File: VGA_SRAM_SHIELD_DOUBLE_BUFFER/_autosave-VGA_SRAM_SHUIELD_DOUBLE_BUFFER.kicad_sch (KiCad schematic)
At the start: 45 parts, among them J1 USB_A_Stacked, J2 ANALOG, J3 Mini-DIN-6, J4 PWR AUX, J5 ISP, J6 Micro_SD_Card, J7 VGA D-SUB15, J8 AUDIO, U1 74HC245, U10 74HC245, U11 74HC245, U12 74LS08, U13 74LS32, U14 DATA_BANK1, U15 DATA_BANK2, U16 74HC245, U17 74HC245, U18 74HC245, U19 K6X8008T2B-TF55, U2 74HC245, U20 K6X8008T2B-TF55, U21 74HC245, U22 74HC245, U3 74HC245, U4 ATF1504AS, U5 74HC245, U6 74HC245, U7 74HC245, U8 74HC14, U9 74HC245, X1 TCXO-14

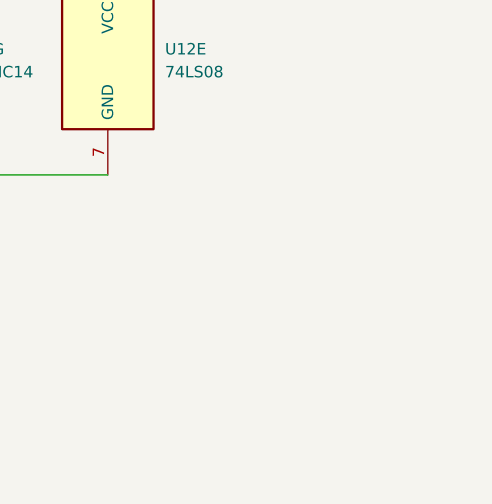
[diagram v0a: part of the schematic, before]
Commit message: remove second vga resistor network
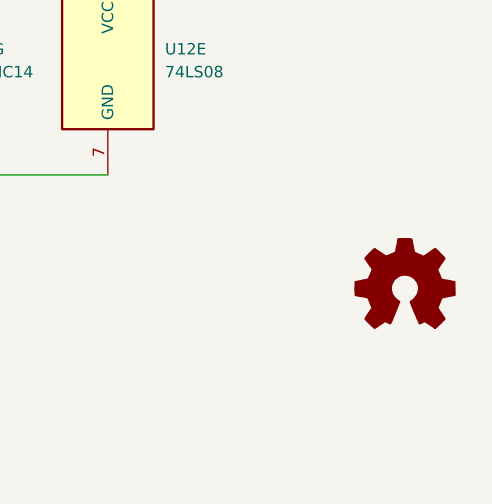
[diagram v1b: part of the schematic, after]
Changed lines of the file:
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@@
+	)
+	(symbol
+		(lib_id "Graphic:Logo_Open_Hardware_Small")
+		(at 571.5 383.54 0)
+		(unit 1)
+		(exclude_from_sim no)
+		(in_bom no)
+		(on_board no)
+		(dnp no)
+		(fields_autoplaced yes)
+		(property "Reference" "#SYM1"
+			(at 571.5 376.555 0)
+			(effects
+				(font
+					(size 1.27 1.27)
+				)
+				(hide yes)
+			)
+		)
+		(property "Value" "Logo_Open_Hardware_Small"
+			(at 571.5 389.255 0)
+			(effects
+				(font
+					(size 1.27 1.27)
+				)
+				(hide yes)
+			)
+		)
+		(property "Footprint" ""
+			(at 571.5 383.54 0)
+			(effects
+				(font
+					(size 1.27 1.27)
+				)
+				(hide yes)
+			)
+		)
+		(property "Datasheet" "~"
+			(at 571.5 383.54 0)
+			(effects
+				(font
+					(size 1.27 1.27)
+				)
+				(hide yes)
+			)
+		)
+		(property "Description" "Open Hardware logo, small"
+			(at 571.5 383.54 0)
+			(effects
+				(font
+					(size 1.27 1.27)
+				)
+				(hide yes)
+			)
+		)
+		(property "Sim.Enable" "0"
+			(at 571.5 383.54 0)
+			(effects
+				(font
+					(size 1.27 1.27)
+				)
+				(hide yes)
+			)
+		)
+		(instances
+			(project ""
+				(path "/507248d0-8b40-4ad4-9bac-d804aed6a845"
+					(reference "#SYM1")
+					(unit 1)
+				)
+			)
+		)
 	)
 	(symbol
